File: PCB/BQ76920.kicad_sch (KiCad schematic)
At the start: 81 parts, among them CN6 WAFER-SH1.0-6PWB, Q1 CSD13381F4, Q10 TP0610K-T1-GE3, Q2 CSD13381F4, Q3 CSD13381F4, Q4 CSD13381F4, Q5 CSD13381F4, Q6 BSC0702LS, Q7 BSC0702LS, Q8 BSC0702LS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

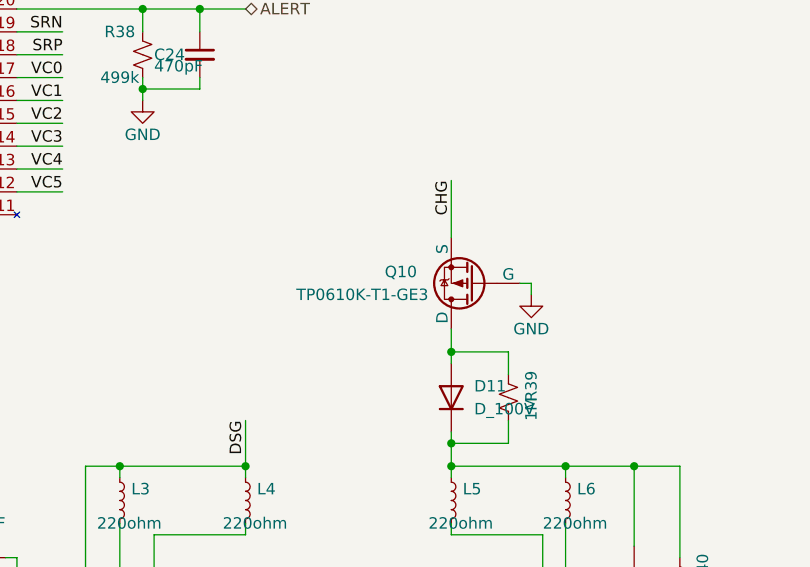
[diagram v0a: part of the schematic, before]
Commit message: 修复充电MOS无法开启的问题
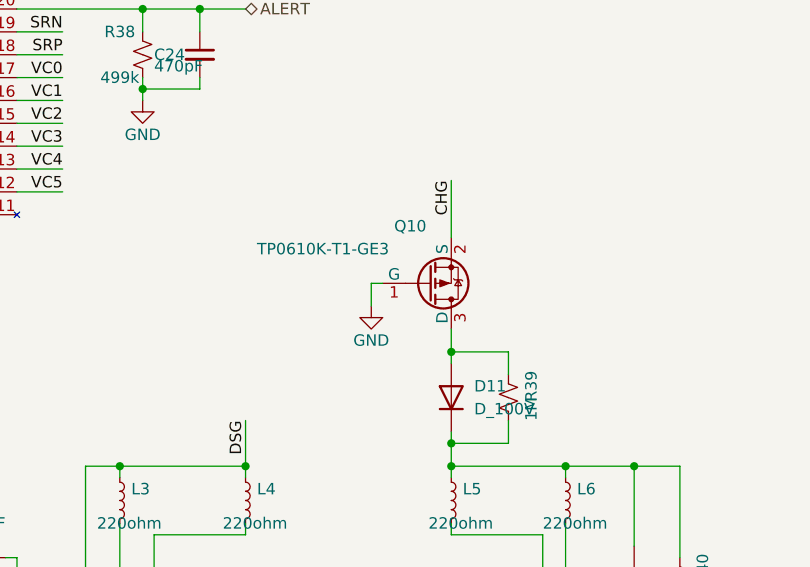
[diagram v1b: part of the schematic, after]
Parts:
- removed Q10: TP0610K-T1-GE3, Package_TO_SOT_SMD:SOT-23, symbol Simulation_SPICE:PMOS
- added Q10: TP0610K-T1-GE3, Package_TO_SOT_SMD:SOT-23, symbol Rick_MOSFET:TP0610K-T1-GE3
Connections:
- net CHG: now also Q10.2 (S)
- net GND: now also Q10.1 (G)
- net at D11.2 (A), R39.2: now also Q10.3 (D)
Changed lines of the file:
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@@
-    (stroke (width 0) (type default))
-  )
-  (wire (pts (xy 217.17 95.25) (xy 217.17 96.52))
     (stroke (width 0) (type default))
   )
@@
     (stroke (width 0) (type default))
   )
+  (wire (pts (xy 199.39 95.25) (xy 199.39 97.79))
+    (stroke (width 0) (type default))
+  )
   (wire (pts (xy 57.15 107.95) (xy 58.42 107.95))
     (stroke (width 0) (type default))
@@
     (stroke (width 0) (type default))
   )
+  (wire (pts (xy 200.66 95.25) (xy 199.39 95.25))
+    (stroke (width 0) (type default))
+  )
   (wire (pts (xy 199.39 132.08) (xy 199.39 134.62))
     (stroke (width 0) (type default))
@@
   )
   (wire (pts (xy 152.4 116.84) (xy 152.4 125.73))
-    (stroke (width 0) (type default))
-  )
-  (wire (pts (xy 215.9 95.25) (xy 217.17 95.25))
     (stroke (width 0) (type default))
   )
@@
     )
   )
-  (symbol (lib_id "Simulation_SPICE:PMOS") (at 210.82 95.25 180) (unit 1)
-    (in_bom yes) (on_board yes) (dnp no)
-    (property "Reference" "Q10" (at 204.47 93.98 0)
-      (effects (font (size 1.27 1.27)) (justify left))
-    )
-    (property "Value" "TP0610K-T1-GE3" (at 205.74 96.52 0)
-      (effects (font (size 1.27 1.27)) (justify left))
-    )
-    (property "Footprint" "Package_TO_SOT_SMD:SOT-23" (at 205.74 97.79 0)
-      (effects (font (size 1.27 1.27)) hide)
-    )
-    (property "Datasheet" "https://ngspice.sourceforge.io/docs/ngspice-manual.pdf" (at 210.82 82.55 0)
-      (effects (font (size 1.27 1.27)) hide)
-    )
-    (property "Sim.Device" "PMOS" (at 210.82 78.105 0)
-      (effects (font (size 1.27 1.27)) hide)
-    )
-    (property "Sim.Type" "VDMOS" (at 210.82 76.2 0)
-      (effects (font (size 1.27 1.27)) hide)
-    )
-    (property "Sim.Pins" "1=D 2=G 3=S" (at 210.82 80.01 0)
-      (effects (font (size 1.27 1.27)) hide)
-    )
-    (pin "1")
-    (pin "2")
-    (pin "3")
-    (instances
-      (project "CawBMS"
-        (path "/4a89dd5e-80e0-469e-b1bd-d2c2db4c0387/7188767d-625f-4b5b-9b89-63af2d6cd4b0"
-          (reference "Q10") (unit 1)
-        )
-      )
-    )
-  )
   (symbol (lib_id "Rick_MOSFET:CSD13381F4") (at 49.53 72.39 0) (mirror y) (unit 1)
     (in_bom yes) (on_board yes) (dnp no)
@@
     )
   )
+  (symbol (lib_id "Rick_MOSFET:TP0610K-T1-GE3") (at 205.74 95.25 0) (mirror x) (unit 1)
+    (in_bom yes) (on_board yes) (dnp no)
+    (property "Reference" "Q10" (at 201.93 88.9 0)
+      (effects (font (size 1.27 1.27)) (justify left))
+    )
+    (property "Value" "TP0610K-T1-GE3" (at 186.69 91.44 0)
+      (effects (font (size 1.27 1.27)) (justify left))
+    )
+    (property "Footprint" "Package_TO_SOT_SMD:SOT-23" (at 210.82 97.79 0)
+      (effects (font (size 1.27 1.27)) hide)
+    )
+    (property "Datasheet" "https://ngspice.sourceforge.io/docs/ngspice-manual.pdf" (at 205.74 82.55 0)
+      (effects (font (size 1.27 1.27)) hide)
+    )
+    (property "Sim.Device" "PMOS" (at 205.74 78.105 0)
+      (effects (font (size 1.27 1.27)) hide)
+    )
+    (property "Sim.Type" "VDMOS" (at 205.74 76.2 0)
+      (effects (font (size 1.27 1.27)) hide)
+    )
+    (property "Sim.Pins" "1=D 2=G 3=S" (at 205.74 80.01 0)
+      (effects (font (size 1.27 1.27)) hide)
+    )
+    (pin "1")
+    (pin "2")
+    (pin "3")
+    (instances
+      (project "CawBMS"
+        (path "/4a89dd5e-80e0-469e-b1bd-d2c2db4c0387/7188767d-625f-4b5b-9b89-63af2d6cd4b0"
+          (reference "Q10") (unit 1)
+        )
+      )
+    )
+  )
   (symbol (lib_id "Device:L_Small") (at 171.45 119.38 0) (unit 1)
     (in_bom yes) (on_board yes) (dnp no)
@@
     )
   )
-  (symbol (lib_id "power:GND") (at 217.17 96.52 0) (unit 1)
-    (in_bom yes) (on_board yes) (dnp no)
-    (property "Reference" "#PWR053" (at 217.17 102.87 0)
-      (effects (font (size 1.27 1.27)) hide)
-    )
-    (property "Value" "GND" (at 217.17 100.33 0)
-      (effects (font (size 1.27 1.27)))
-    )
-    (property "Footprint" "" (at 217.17 96.52 0)
-      (effects (font (size 1.27 1.27)) hide)
-    )
-    (property "Datasheet" "" (at 217.17 96.52 0)
-      (effects (font (size 1.27 1.27)) hide)
-    )
+  (symbol (lib_id "power:GND") (at 199.39 97.79 0) (unit 1)
+    (in_bom yes) (on_board yes) (dnp no)
+    (property "Reference" "#PWR053" (at 199.39 104.14 0)
+      (effects (font (size 1.27 1.27)) hide)
+    )
+    (property "Value" "GND" (at 199.39 101.6 0)
+      (effects (font (size 1.27 1.27)))
+    )
+    (property "Footprint" "" (at 199.39 97.79 0)
+      (effects (font (size 1.27 1.27)) hide)
+    )
+    (property "Datasheet" "" (at 199.39 97.79 0)
+      (effects (font (size 1.27 1.27)) hide)
+    )
